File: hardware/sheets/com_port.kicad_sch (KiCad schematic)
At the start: 27 parts, among them J1 DE9_Pins, J2 Conn_01x03, J3 Conn_01x04, U1 16550, U2 MAX3241, U3 74HCT04, U4 74HCT08, U5 74HCT08, U6 74HCT125, Y1 1.8432MHz

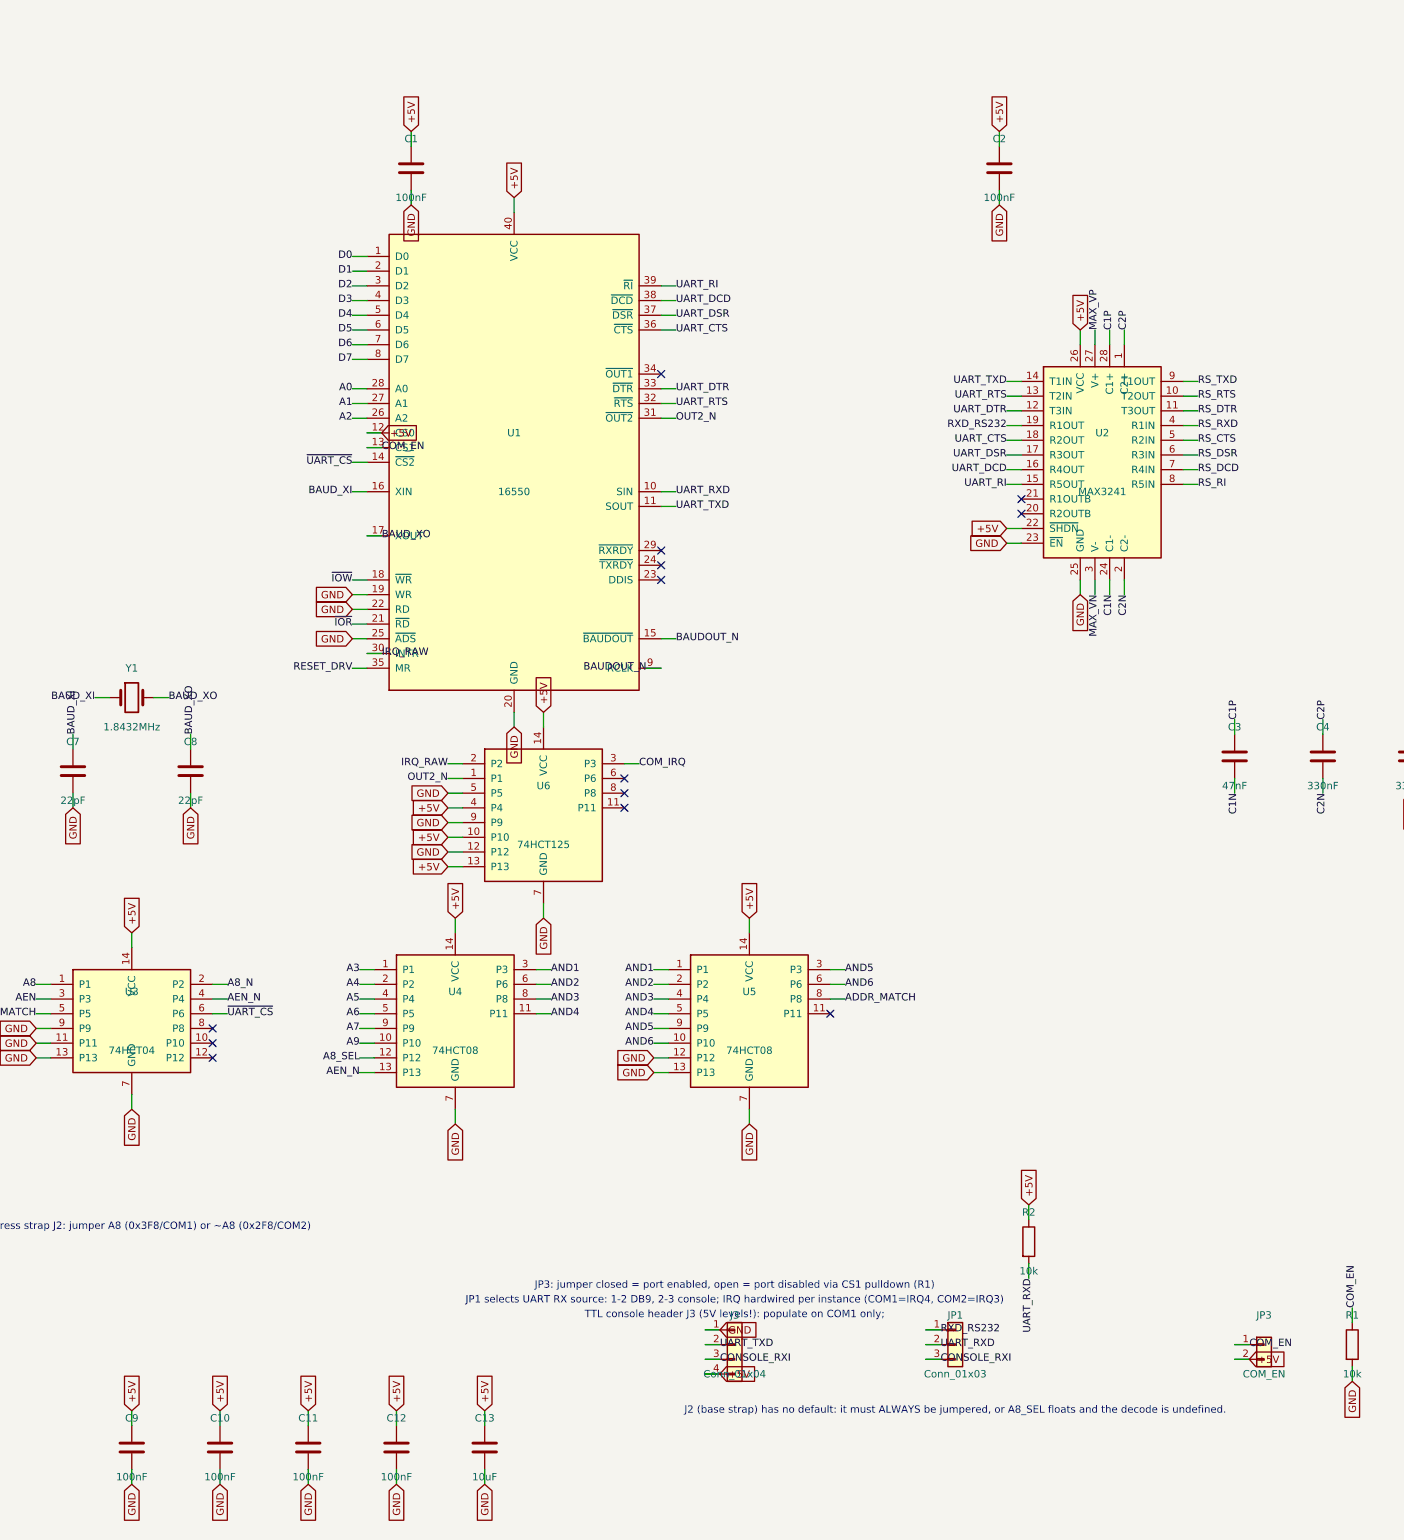
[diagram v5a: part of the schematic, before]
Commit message: com/network/storage/parallel: 3.3V; TL16C550CPT soldered; LVC at external connectors
com_port: PLCC-44 16550 socket -> soldered TL16C550PT (LQFP-48) at +3V3,
rewired signal-for-signal from pins.py (RD/WR split renamed RD1/RD2/WR1/WR2,
INTR->INTRPT, GND->VSS, 8 new NC pins). Decode glue -> HC-grade, IRQ buffer
-> LVC125A, all +3V3. MAX3241 untouched (+5V, spec: already 3.3V-compatible).

network: only U3 (IRQ/AEN gate) moves, to LVC125A @ +3V3 -- RTL8019AS and
its EEPROM stay +5V (datasheet-verified 5V-only part, same treatment as
MAX3241), deviating from a literal reading of the brief's "power sweep"
instruction in favor of its own MAX3241 precedent.

storage: full brief table applied, all +3V3 except the CompactFlash
socket's own VCC power-feed pins (real CF-spec requirement, not a logic
signal).

parallel: brief's swap table only named 8 of 13 chips; traced the DB25
connector's actual net fan-out to fill the gap (U5, U9 also need
5V-tolerant inputs; U6/U7/U8/U12 are purely internal decode -> HC-grade).
U9 reuses the already-bound 74AHC14 value (no bare LVC04A entry exists).

Decisions logged in hardware/notes/questions-{com_port,network,storage,parallel}.md.

Co-Authored-By: Claude Fable 5 <noreply@anthropic.com>
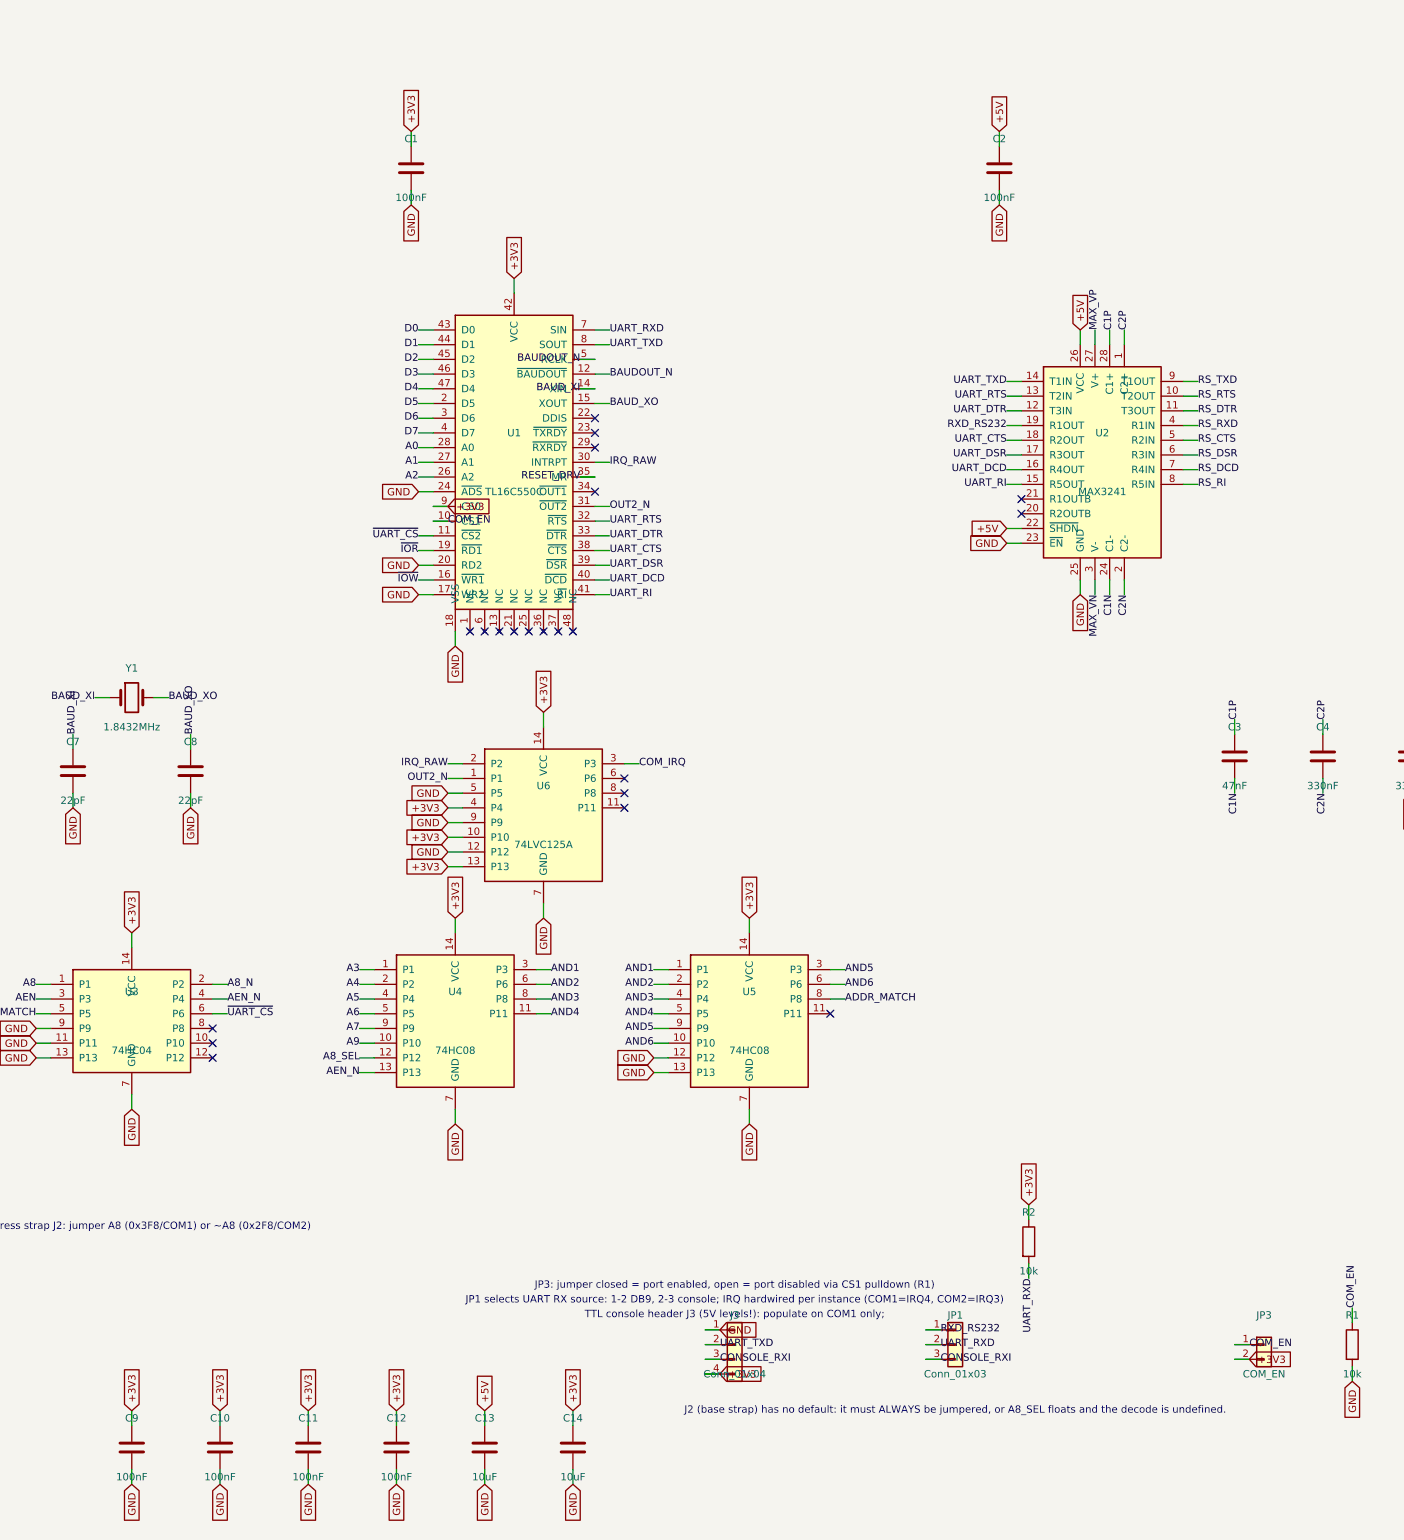
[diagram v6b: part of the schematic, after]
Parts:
- added C14: 10uF, Capacitor_SMD:C_0805_2012Metric, symbol Device:C
- U1: value 16550 -> TL16C550C; footprint (none) -> Package_QFP:LQFP-48_7x7mm_P0.5mm; symbol Interface_UART:16550 -> mini-xt:TL16C550PT
- U3: value 74HCT04 -> 74HC04; LCSC Part Num C672096 -> C86613
- U4, U5: value 74HCT08 -> 74HC08; LCSC Part Num C5959 -> C5593
- U6: value 74HCT125 -> 74LVC125A; LCSC Part Num C5962 -> C6057
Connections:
- net +5V: no longer C1.1, C10.1, C11.1, C12.1, C9.1, J3.4 (Pin_4), JP3.2 (Pin_2), R2.1, U1.12 (CS0), U1.40 (VCC), U3.14 (VCC), U4.14 (VCC), U5.14 (VCC), U6.10 (P10), U6.13 (P13), U6.14 (VCC), U6.4 (P4)
- net BAUDOUT_N: now also U1.12 (~{BAUDOUT}), U1.5 (RCLK); no longer U1.15 (~{BAUDOUT}), U1.9 (RCLK)
- net BAUD_XI: now also U1.14 (XIN); no longer U1.16 (XIN)
- net BAUD_XO: now also U1.15 (XOUT); no longer U1.17 (XOUT)
- net COM_EN: now also U1.10 (CS1); no longer U1.13 (CS1)
- net D0: now also U1.43 (D0); no longer U1.1 (D0)
- net D1: now also U1.44 (D1); no longer U1.2 (D1)
- net D2: now also U1.45 (D2); no longer U1.3 (D2)
- net D3: now also U1.46 (D3); no longer U1.4 (D3)
- net D4: now also U1.47 (D4); no longer U1.5 (D4)
- net D5: now also U1.2 (D5); no longer U1.6 (D5)
- net D6: now also U1.3 (D6); no longer U1.7 (D6)
- net D7: now also U1.4 (D7); no longer U1.8 (D7)
- net GND: now also U1.17 (WR2), U1.18 (VSS), U1.24 (~{ADS}), C14.2; no longer U1.19 (WR), U1.22 (RD), U1.25 (~{ADS})
- net UART_CTS: now also U1.38 (~{CTS}); no longer U1.36 (~{CTS})
- net UART_DCD: now also U1.40 (~{DCD}); no longer U1.38 (~{DCD})
- net UART_DSR: now also U1.39 (~{DSR}); no longer U1.37 (~{DSR})
- net UART_RI: now also U1.41 (~{RI}); no longer U1.39 (~{RI})
- net UART_RXD: now also U1.7 (SIN); no longer U1.10 (SIN)
- net UART_TXD: now also U1.8 (SOUT); no longer U1.11 (SOUT)
- net ~{IOR}: now also U1.19 (~{RD1}); no longer U1.21 (~{RD})
- net ~{IOW}: now also U1.16 (~{WR1}); no longer U1.18 (~{WR})
- net ~{UART_CS}: now also U1.11 (~{CS2}); no longer U1.14 (~{CS2})
- new net +3V3: C1.1, C10.1, C11.1, C12.1, C14.1, C9.1, J3.4 (Pin_4), JP3.2 (Pin_2), R2.1, U1.42 (VCC), U1.9 (CS0), U3.14 (VCC), U4.14 (VCC), U5.14 (VCC), U6.10 (P10), U6.13 (P13), U6.14 (VCC), U6.4 (P4)
- no-connect marks 13 -> 21
